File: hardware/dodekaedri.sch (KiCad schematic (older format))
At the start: 13 parts

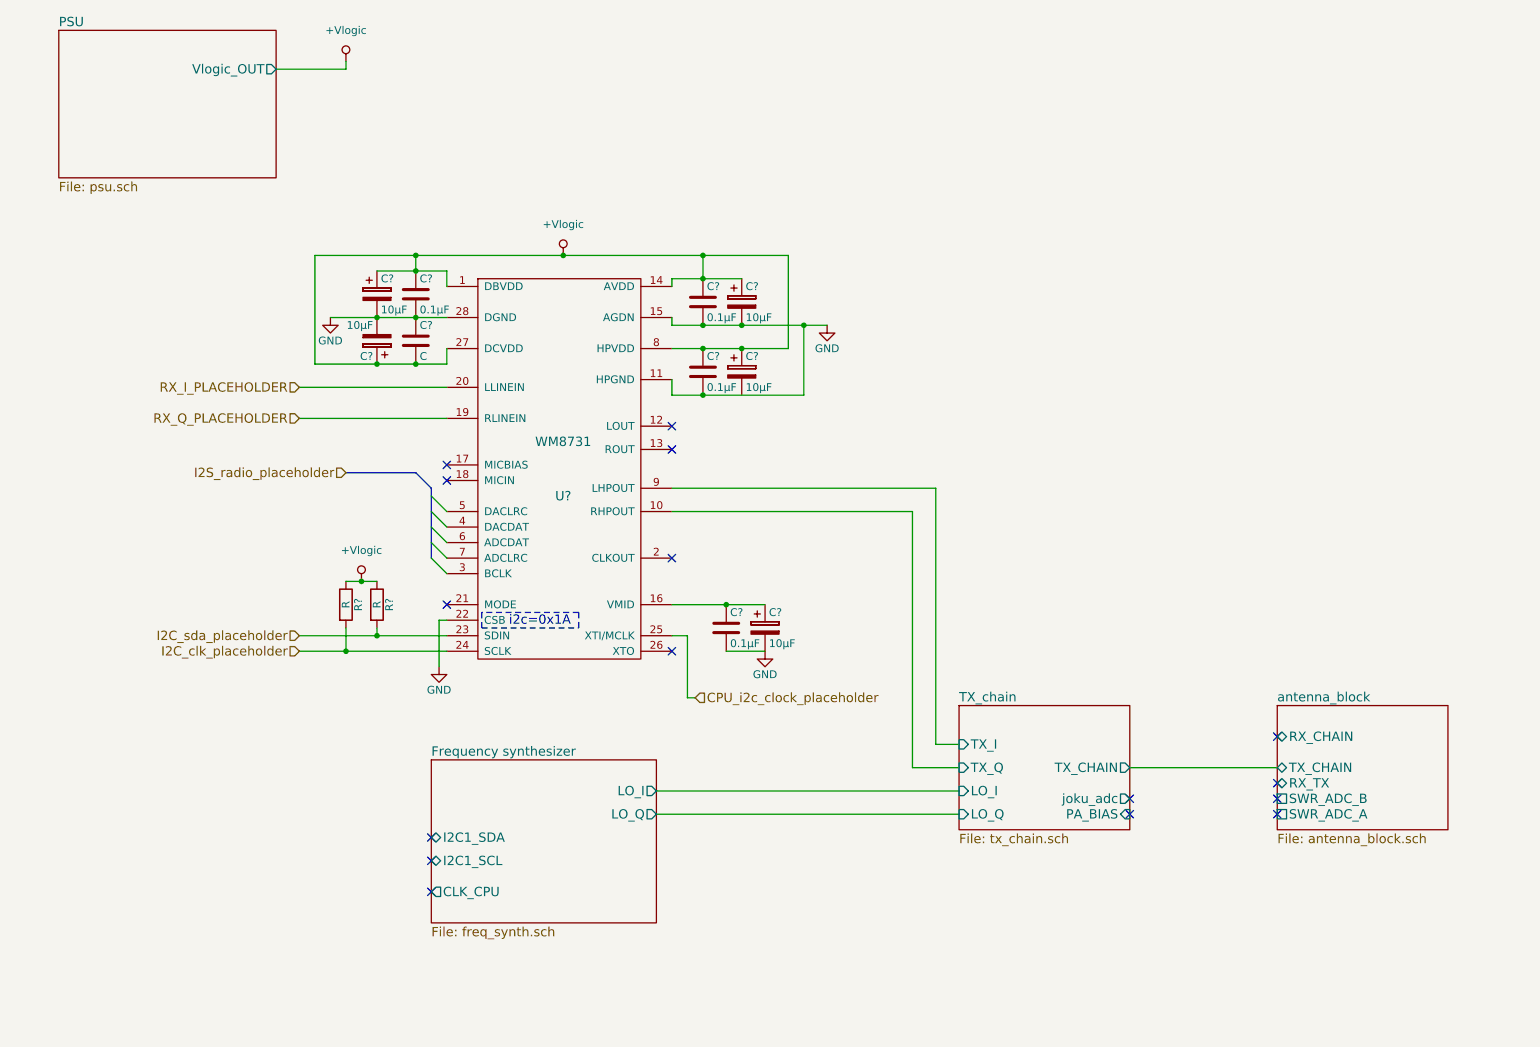
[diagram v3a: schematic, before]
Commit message: Added RX chain. also modified and cleand up other schemas
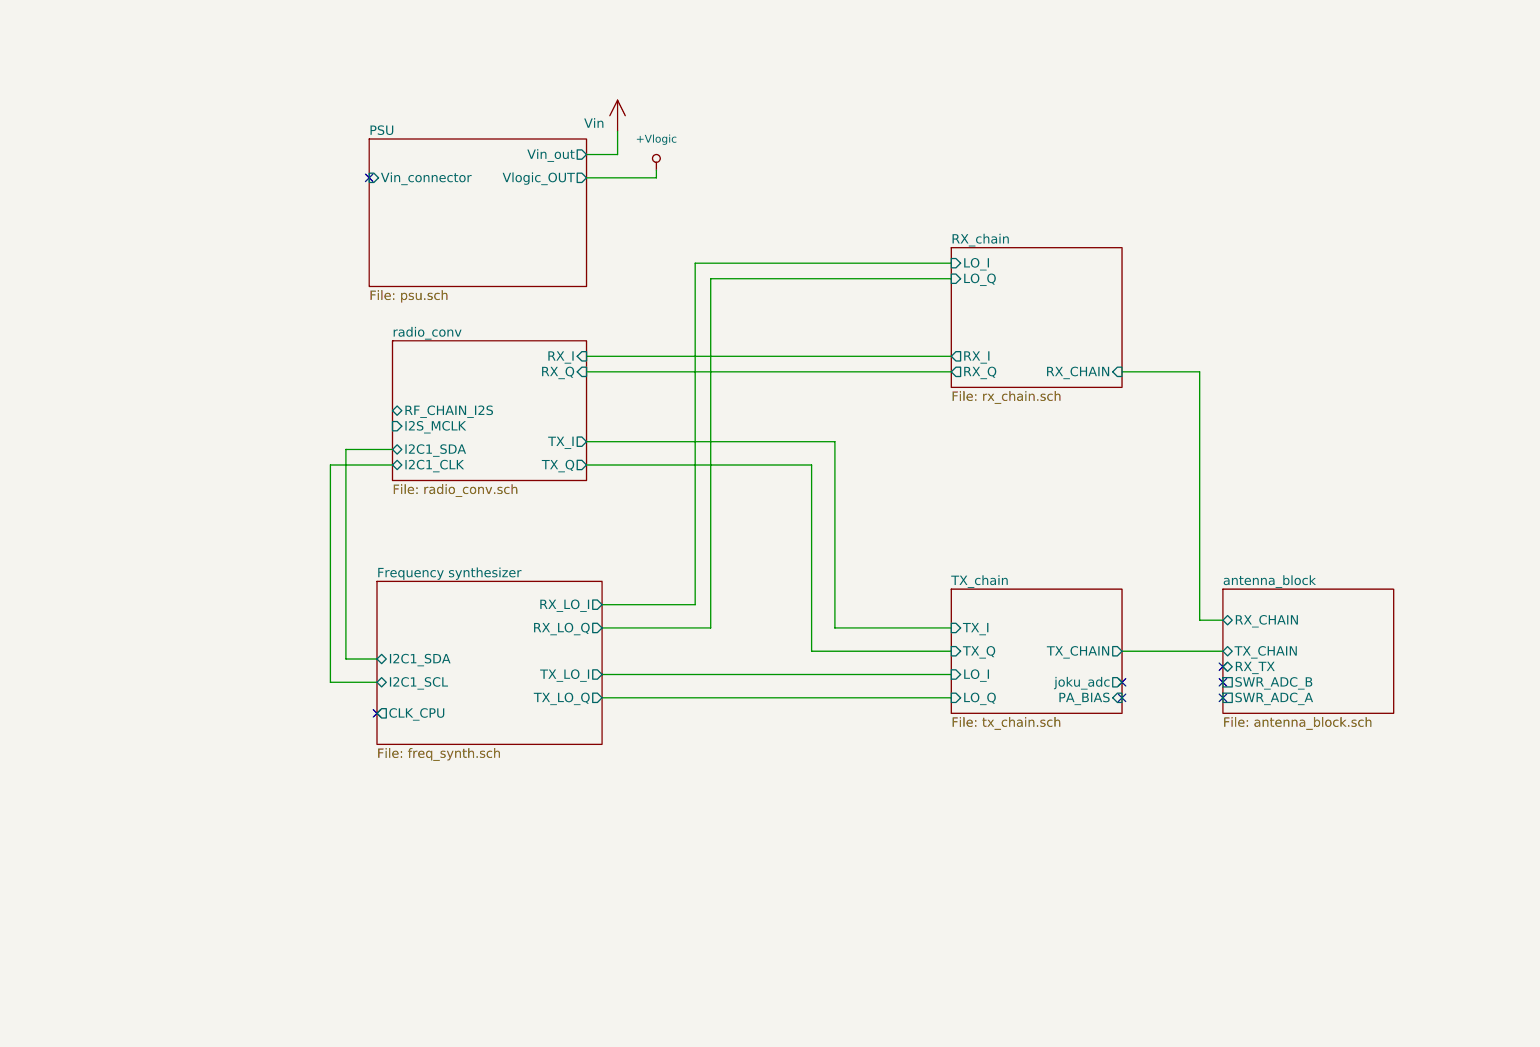
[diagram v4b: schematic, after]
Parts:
- removed C? (x5): 10µF, symbol CP
- removed C? (x4): 0.1µF, symbol C
- removed C?: C, symbol C
- removed R? (x2): R, symbol R
- removed U?: WM8731, symbol WM8731
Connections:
- no-connect marks 16 -> 7
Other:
- note removed: "i2c=0x1A"

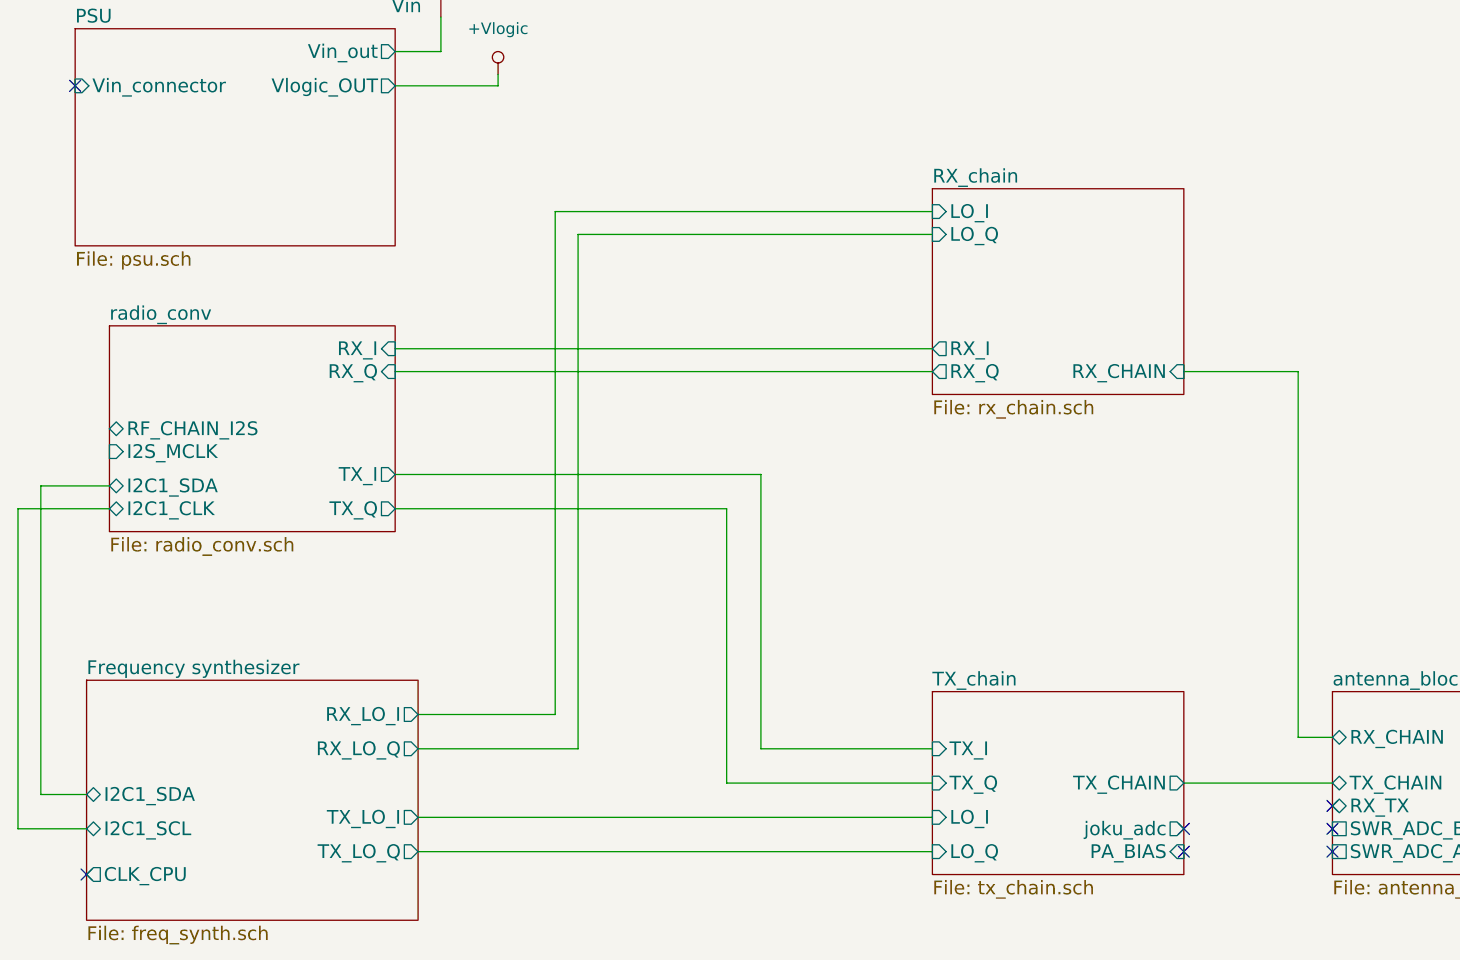
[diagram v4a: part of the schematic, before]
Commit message: Added biases for RX and TX chains where needed
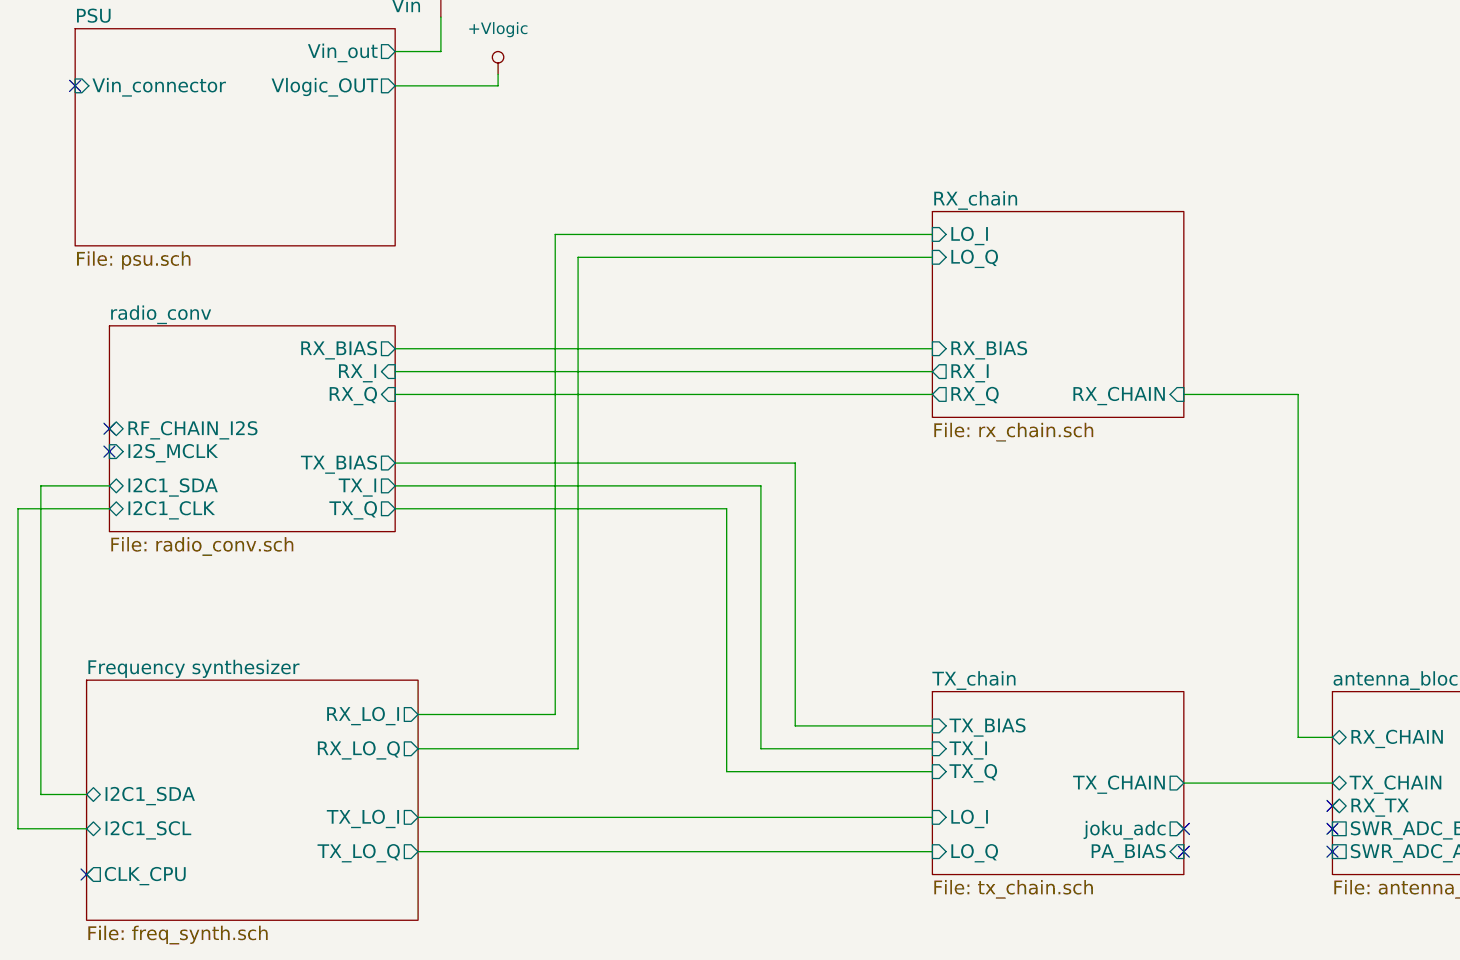
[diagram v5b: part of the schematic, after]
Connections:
- no-connect marks 7 -> 9
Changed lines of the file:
@@
 Comp "PRK - OH2TI"
 Comment1 "exla - OH2EHK"
-Comment2 ""
+Comment2 "tejeez - OH2EAT"
 Comment3 ""
 Comment4 ""
@@
 F1 "tx_chain.sch" 60
 F2 "TX_I" I L 6900 4850 60
-F3 "TX_Q" I L 6900 5000 60
+F3 "TX_Q" I L 6900 4950 60
 F4 "LO_I" I L 6900 5150 60
 F5 "LO_Q" I L 6900 5300 60
@@
 F7 "TX_CHAIN" O R 8000 5000 60
 F8 "joku_adc" O R 8000 5200 60
+F9 "TX_BIAS" I L 6900 4750 60
 $EndSheet
 NoConn ~ 3200 5400
@@
 NoConn ~ 8650 5300
 $Sheet
-S 6900 2400 1100 900
+S 6900 2500 1100 900
 U 57E4503B
 F0 "RX_chain" 60
 F1 "rx_chain.sch" 60
-F2 "RX_CHAIN" I R 8000 3200 60
-F3 "LO_I" I L 6900 2500 60
-F4 "LO_Q" I L 6900 2600 60
-F5 "RX_I" O L 6900 3100 60
-F6 "RX_Q" O L 6900 3200 60
-$EndSheet
-$Sheet
-S 3300 3000 1250 900
-U 57E49662
-F0 "radio_conv" 60
-F1 "radio_conv.sch" 60
-F2 "RF_CHAIN_I2S" B L 3300 3450 60
-F3 "I2C1_SDA" B L 3300 3700 60
-F4 "I2C1_CLK" B L 3300 3800 60
-F5 "I2S_MCLK" I L 3300 3550 60
-F6 "RX_I" I R 4550 3100 60
-F7 "RX_Q" I R 4550 3200 60
-F8 "TX_I" O R 4550 3650 60
-F9 "TX_Q" O R 4550 3800 60
+F2 "RX_CHAIN" I R 8000 3300 60
+F3 "LO_I" I L 6900 2600 60
+F4 "LO_Q" I L 6900 2700 60
+F5 "RX_I" O L 6900 3200 60
+F6 "RX_Q" O L 6900 3300 60
+F7 "RX_BIAS" I L 6900 3100 60
 $EndSheet
 Wire Wire Line
@@
 	6150 4850 6900 4850
 Wire Wire Line
-	6000 5000 6900 5000
+	6000 4950 6900 4950
 Wire Wire Line
 	4650 5150 6900 5150
@@
 	4550 3800 6000 3800
 Wire Wire Line
-	6000 3800 6000 5000
+	6000 3800 6000 4950
 Wire Wire Line
-	6150 4850 6150 3650
+	6150 4850 6150 3700
 Wire Wire Line
-	6150 3650 4550 3650
+	6150 3700 4550 3700
 Wire Wire Line
 	3300 3700 3000 3700
@@
 	2900 5200 3200 5200
 Wire Wire Line
-	5250 2500 6900 2500
+	5250 2600 6900 2600
 Wire Wire Line
-	5350 2600 6900 2600
+	5350 2700 6900 2700
 Wire Wire Line
-	8000 3200 8500 3200
+	8000 3300 8500 3300
 Wire Wire Line
-	8500 3200 8500 4800
+	8500 3300 8500 4800
 Wire Wire Line
 	8500 4800 8650 4800
 Wire Wire Line
-	4550 3100 6900 3100
+	4550 3200 6900 3200
 Wire Wire Line
-	4550 3200 6900 3200
+	4550 3300 6900 3300
 Wire Wire Line
 	4650 4700 5250 4700
 Wire Wire Line
-	5250 4700 5250 2500
+	5250 4700 5250 2600
 Wire Wire Line
-	5350 2600 5350 4850
+	5350 2700 5350 4850
 Wire Wire Line
 	5350 4850 4650 4850
@@
 Wire Wire Line
 	4750 1800 4750 1650
+NoConn ~ 3300 3450
+NoConn ~ 3300 3550
+$Sheet
+S 3300 3000 1250 900
+U 57E49662
+F0 "radio_conv" 60
+F1 "radio_conv.sch" 60
+F2 "RF_CHAIN_I2S" B L 3300 3450 60
+F3 "I2C1_SDA" B L 3300 3700 60
+F4 "I2C1_CLK" B L 3300 3800 60
+F5 "I2S_MCLK" I L 3300 3550 60
+F6 "RX_I" I R 4550 3200 60
+F7 "RX_Q" I R 4550 3300 60
+F8 "TX_I" O R 4550 3700 60
+F9 "TX_Q" O R 4550 3800 60
+F10 "RX_BIAS" O R 4550 3100 60
+F11 "TX_BIAS" O R 4550 3600 60
+$EndSheet
+Wire Wire Line
+	4550 3100 6900 3100
+Wire Wire Line
+	4550 3600 6300 3600
+Wire Wire Line
+	6300 3600 6300 4750
+Wire Wire Line
+	6300 4750 6900 4750
 $EndSCHEMATC
